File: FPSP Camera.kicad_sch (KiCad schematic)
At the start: 75 parts, among them J101 Conn_01x24_Socket, J102 SM03B-SRSS-TB, J103 USB_B_Micro, J104 Conn_02x06_Odd_Even, U1 ICM-45686, U102 W25Q128JVS, U103 RP2350_60QFN, U104 TLV75533PDRV, U105 TLV73328PDRV, U106 TLV73315PDRV, Y101 SiT8008xx-1x-xxE

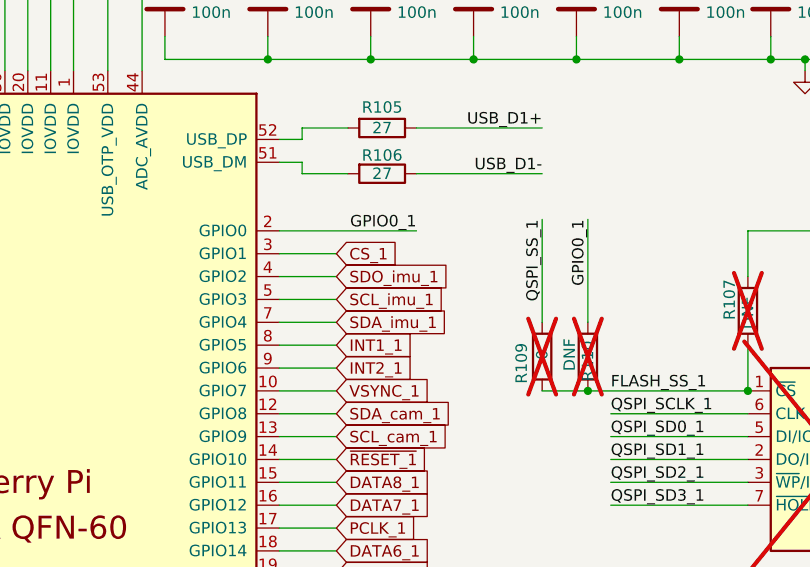
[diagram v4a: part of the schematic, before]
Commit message: IMU Subsystem Change
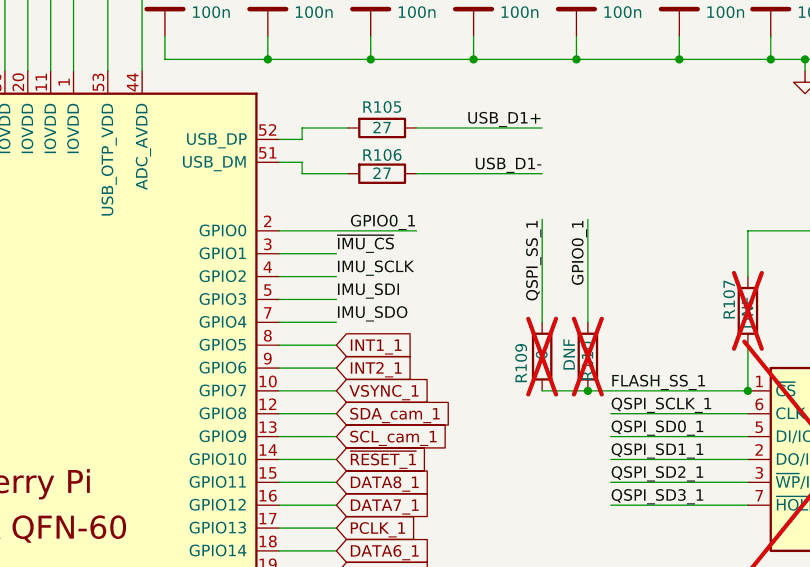
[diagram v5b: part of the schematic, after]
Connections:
- net CS_1 is gone; now on net ~{IMU_CS}: U103.3 (GPIO1)
- net SCL_imu_1 is gone; now on net IMU_SDI: U103.5 (GPIO3)
- net SDA_imu_1 is gone; now on net IMU_SDO: U103.7 (GPIO4)
- net SDO_imu_1 is gone; now on net IMU_SCLK: U103.4 (GPIO2)
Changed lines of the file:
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@@
+		)
+	)
+	(label "~{IMU_CS}"
+		(at 160.02 88.9 0)
+		(effects
+			(font
+				(size 1.27 1.27)
+			)
+			(justify left bottom)
 		)
 	)
@@
 		)
 	)
+	(label "IMU_SDI"
+		(at 160.02 93.98 0)
+		(effects
+			(font
+				(size 1.27 1.27)
+			)
+			(justify left bottom)
+		)
+	)
+	(label "IMU_SCLK"
+		(at 160.02 91.44 0)
+		(effects
+			(font
+				(size 1.27 1.27)
+			)
+			(justify left bottom)
+		)
+	)
 	(label "~{RESET_1}"
 		(at 330.2 113.03 0)
@@
 			)
 			(justify right bottom)
+		)
+	)
+	(label "IMU_SDO"
+		(at 160.02 96.52 0)
+		(effects
+			(font
+				(size 1.27 1.27)
+			)
+			(justify left bottom)
 		)
 	)
@@
 		)
 	)
-	(global_label "SDO_imu_1"
-		(shape input)
-		(at 160.02 91.44 0)
-		(fields_autoplaced yes)
-		(effects
-			(font
-				(size 1.27 1.27)
-			)
-			(justify left)
-		)
-		(property "Intersheetrefs" "${INTERSHEET_REFS}"
-			(at 173.407 91.44 0)
-			(effects
-				(font
-					(size 1.27 1.27)
-				)
-				(justify left)
-				(hide yes)
-			)
-		)
-	)
 	(global_label "SWCLK_1"
 		(shape input)
@@
 				)
 				(justify right)
-				(hide yes)
-			)
-		)
-	)
-	(global_label "SCL_imu_1"
-		(shape input)
-		(at 160.02 93.98 0)
-		(fields_autoplaced yes)
-		(effects
-			(font
-				(size 1.27 1.27)
-			)
-			(justify left)
-		)
-		(property "Intersheetrefs" "${INTERSHEET_REFS}"
-			(at 173.1046 93.98 0)
-			(effects
-				(font
-					(size 1.27 1.27)
-				)
-				(justify left)
 				(hide yes)
 			)
@@
 		)
 	)
-	(global_label "CS_1"
-		(shape input)
-		(at 160.02 88.9 0)
-		(fields_autoplaced yes)
-		(effects
-			(font
-				(size 1.27 1.27)
-			)
-			(justify left)
-		)
-		(property "Intersheetrefs" "${INTERSHEET_REFS}"
-			(at 167.6618 88.9 0)
-			(effects
-				(font
-					(size 1.27 1.27)
-				)
-				(justify left)
-				(hide yes)
-			)
-		)
-	)
 	(global_label "INT2_1"
 		(shape input)
@@
 			(effects
 				(font
-					(size 1.27 1.27)
-				)
-				(justify left)
-				(hide yes)
-			)
-		)
-	)
-	(global_label "SDA_imu_1"
-		(shape input)
-		(at 160.02 96.52 0)
-		(fields_autoplaced yes)
-		(effects
-			(font
-				(size 1.27 1.27)
-			)
-			(justify left)
-		)
-		(property "Intersheetrefs" "${INTERSHEET_REFS}"
-			(at 173.1651 96.52 0)
-			(effects
-				(font
